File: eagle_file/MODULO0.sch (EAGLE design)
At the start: 3 parts

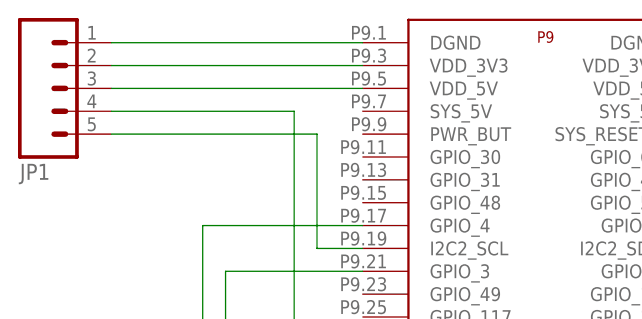
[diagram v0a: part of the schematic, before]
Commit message: GND to MODULO0
Ho messo a massa il Modulo0
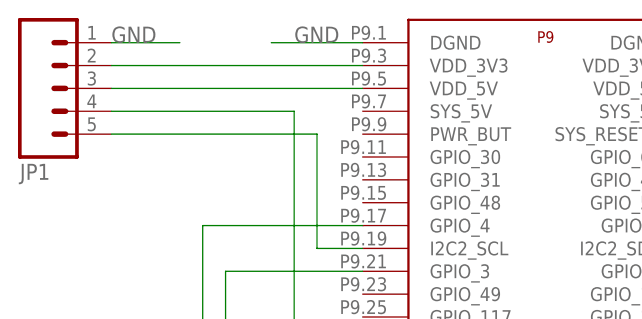
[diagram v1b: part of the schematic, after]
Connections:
- net N$1 renamed GND
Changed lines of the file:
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@@
 <?xml version="1.0" encoding="utf-8"?>
 <!DOCTYPE eagle SYSTEM "eagle.dtd">
-<eagle version="7.3.0">
+<eagle version="7.1.0">
 <drawing>
 <settings>
@@
 </busses>
 <nets>
-<net name="N$1" class="0">
-<segment>
-<pinref part="JP1" gate="G$1" pin="1"/>
-<pinref part="U$1" gate="P9" pin="DGND@1"/>
-<wire x1="50.8" y1="71.12" x2="78.74" y2="71.12" width="0.1524" layer="91"/>
-</segment>
-</net>
 <net name="N$2" class="0">
 <segment>
@@
 </segment>
 </net>
+<net name="GND" class="0">
+<segment>
+<pinref part="JP1" gate="G$1" pin="1"/>
+<wire x1="50.8" y1="71.12" x2="58.42" y2="71.12" width="0.1524" layer="91"/>
+<label x="50.8" y="71.12" size="1.778" layer="95"/>
+</segment>
+<segment>
+<pinref part="U$1" gate="P9" pin="DGND@1"/>
+<wire x1="78.74" y1="71.12" x2="68.58" y2="71.12" width="0.1524" layer="91"/>
+<label x="71.12" y="71.12" size="1.778" layer="95"/>
+</segment>
+</net>

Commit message: Modulo1
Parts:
- JP2: device SparkFun-Connectors:M06LOCK -> SparkFun-Connectors:M06SILK_FEMALE_PTH
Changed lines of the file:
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@@
 <grid distance="0.1" unitdist="inch" unit="inch" style="lines" multiple="1" display="no" altdistance="0.01" altunitdist="inch" altunit="inch"/>
 <layers>
-<layer number="1" name="Top" color="4" fill="1" visible="no" active="no"/>
-<layer number="16" name="Bottom" color="1" fill="1" visible="no" active="no"/>
-<layer number="17" name="Pads" color="2" fill="1" visible="no" active="no"/>
-<layer number="18" name="Vias" color="2" fill="1" visible="no" active="no"/>
-<layer number="19" name="Unrouted" color="6" fill="1" visible="no" active="no"/>
-<layer number="20" name="Dimension" color="15" fill="1" visible="no" active="no"/>
-<layer number="21" name="tPlace" color="16" fill="1" visible="no" active="no"/>
-<layer number="22" name="bPlace" color="14" fill="1" visible="no" active="no"/>
-<layer number="23" name="tOrigins" color="15" fill="1" visible="no" active="no"/>
-<layer number="24" name="bOrigins" color="15" fill="1" visible="no" active="no"/>
-<layer number="25" name="tNames" color="7" fill="1" visible="no" active="no"/>
-<layer number="26" name="bNames" color="7" fill="1" visible="no" active="no"/>
-<layer number="27" name="tValues" color="7" fill="1" visible="no" active="no"/>
-<layer number="28" name="bValues" color="7" fill="1" visible="no" active="no"/>
+<layer number="1" name="Top" color="4" fill="1" visible="yes" active="no"/>
+<layer number="16" name="Bottom" color="1" fill="1" visible="yes" active="no"/>
+<layer number="17" name="Pads" color="2" fill="1" visible="yes" active="no"/>
+<layer number="18" name="Vias" color="2" fill="1" visible="yes" active="no"/>
+<layer number="19" name="Unrouted" color="6" fill="1" visible="yes" active="no"/>
+<layer number="20" name="Dimension" color="15" fill="1" visible="yes" active="no"/>
+<layer number="21" name="tPlace" color="7" fill="1" visible="yes" active="no"/>
+<layer number="22" name="bPlace" color="7" fill="1" visible="yes" active="no"/>
+<layer number="23" name="tOrigins" color="15" fill="1" visible="yes" active="no"/>
+<layer number="24" name="bOrigins" color="15" fill="1" visible="yes" active="no"/>
+<layer number="25" name="tNames" color="7" fill="1" visible="yes" active="no"/>
+<layer number="26" name="bNames" color="7" fill="1" visible="yes" active="no"/>
+<layer number="27" name="tValues" color="7" fill="1" visible="yes" active="no"/>
+<layer number="28" name="bValues" color="7" fill="1" visible="yes" active="no"/>
 <layer number="29" name="tStop" color="7" fill="3" visible="no" active="no"/>
 <layer number="30" name="bStop" color="7" fill="6" visible="no" active="no"/>
@@
 <layer number="35" name="tGlue" color="7" fill="4" visible="no" active="no"/>
 <layer number="36" name="bGlue" color="7" fill="5" visible="no" active="no"/>
-<layer number="37" name="tTest" color="7" fill="1" visible="no" active="no"/>
-<layer number="38" name="bTest" color="7" fill="1" visible="no" active="no"/>
+<layer number="37" name="tTest" color="7" fill="1" visible="yes" active="no"/>
+<layer number="38" name="bTest" color="7" fill="1" visible="yes" active="no"/>
 <layer number="39" name="tKeepout" color="4" fill="11" visible="no" active="no"/>
 <layer number="40" name="bKeepout" color="1" fill="11" visible="no" active="no"/>
@@
 <layer number="44" name="Drills" color="7" fill="1" visible="no" active="no"/>
 <layer number="45" name="Holes" color="7" fill="1" visible="no" active="no"/>
-<layer number="46" name="Milling" color="3" fill="1" visible="no" active="no"/>
-<layer number="47" name="Measures" color="7" fill="1" visible="no" active="no"/>
-<layer number="48" name="Document" color="7" fill="1" visible="no" active="no"/>
-<layer number="49" name="Reference" color="7" fill="1" visible="no" active="no"/>
-<layer number="50" name="dxf" color="7" fill="1" visible="no" active="no"/>
-<layer number="51" name="tDocu" color="7" fill="1" visible="no" active="no"/>
-<layer number="52" name="bDocu" color="7" fill="1" visible="no" active="no"/>
-<layer number="53" name="tGND_GNDA" color="7" fill="9" visible="no" active="no"/>
-<layer number="54" name="bGND_GNDA" color="1" fill="9" visible="no" active="no"/>
-<layer number="56" name="wert" color="7" fill="1" visible="no" active="no"/>
-<layer number="57" name="tCAD" color="7" fill="1" visible="no" active="no"/>
-<layer number="59" name="tCarbon" color="7" fill="1" visible="no" active="no"/>
-<layer number="60" name="bCarbon" color="7" fill="1" visible="no" active="no"/>
+<layer number="46" name="Milling" color="3" fill="1" visible="yes" active="no"/>
+<layer number="47" name="Measures" color="7" fill="1" visible="yes" active="no"/>
+<layer number="48" name="Document" color="7" fill="1" visible="yes" active="no"/>
+<layer number="49" name="Reference" color="7" fill="1" visible="yes" active="no"/>
+<layer number="50" name="dxf" color="7" fill="1" visible="yes" active="no"/>
+<layer number="51" name="tDocu" color="7" fill="1" visible="yes" active="no"/>
+<layer number="52" name="bDocu" color="7" fill="1" visible="yes" active="no"/>
+<layer number="53" name="tGND_GNDA" color="7" fill="9" visible="yes" active="no"/>
+<layer number="54" name="bGND_GNDA" color="1" fill="9" visible="yes" active="no"/>
+<layer number="56" name="wert" color="7" fill="1" visible="yes" active="no"/>
+<layer number="57" name="tCAD" color="7" fill="1" visible="yes" active="no"/>
+<layer number="59" name="tCarbon" color="7" fill="1" visible="yes" active="no"/>
+<layer number="60" name="bCarbon" color="7" fill="1" visible="yes" active="no"/>
 <layer number="90" name="Modules" color="5" fill="1" visible="yes" active="yes"/>
 <layer number="91" name="Nets" color="2" fill="1" visible="yes" active="yes"/>
@@
 <part name="U$1" library="SparkFun-Boards" deviceset="BEAGLE_BONE_BLACK_CAPE" device=""/>
 <part name="JP1" library="SparkFun-Connectors" deviceset="M05" device="PTH"/>
-<part name="JP2" library="SparkFun-Connectors" deviceset="M06" device="LOCK"/>
+<part name="JP2" library="SparkFun-Connectors" deviceset="M06" device="SILK_FEMALE_PTH"/>
 </parts>
 <sheets>
@@
 </plain>
 <instances>
-<instance part="U$1" gate="P8" x="215.9" y="45.72"/>
 <instance part="U$1" gate="P9" x="99.06" y="45.72"/>
 <instance part="JP1" gate="G$1" x="43.18" y="66.04" rot="MR180"/>
